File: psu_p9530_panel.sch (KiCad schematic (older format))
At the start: 56 parts, among them IC306 LTC1658, IC308 CD4052B, IC310 TLC272, IC312 TLC272, U401 74HCT164

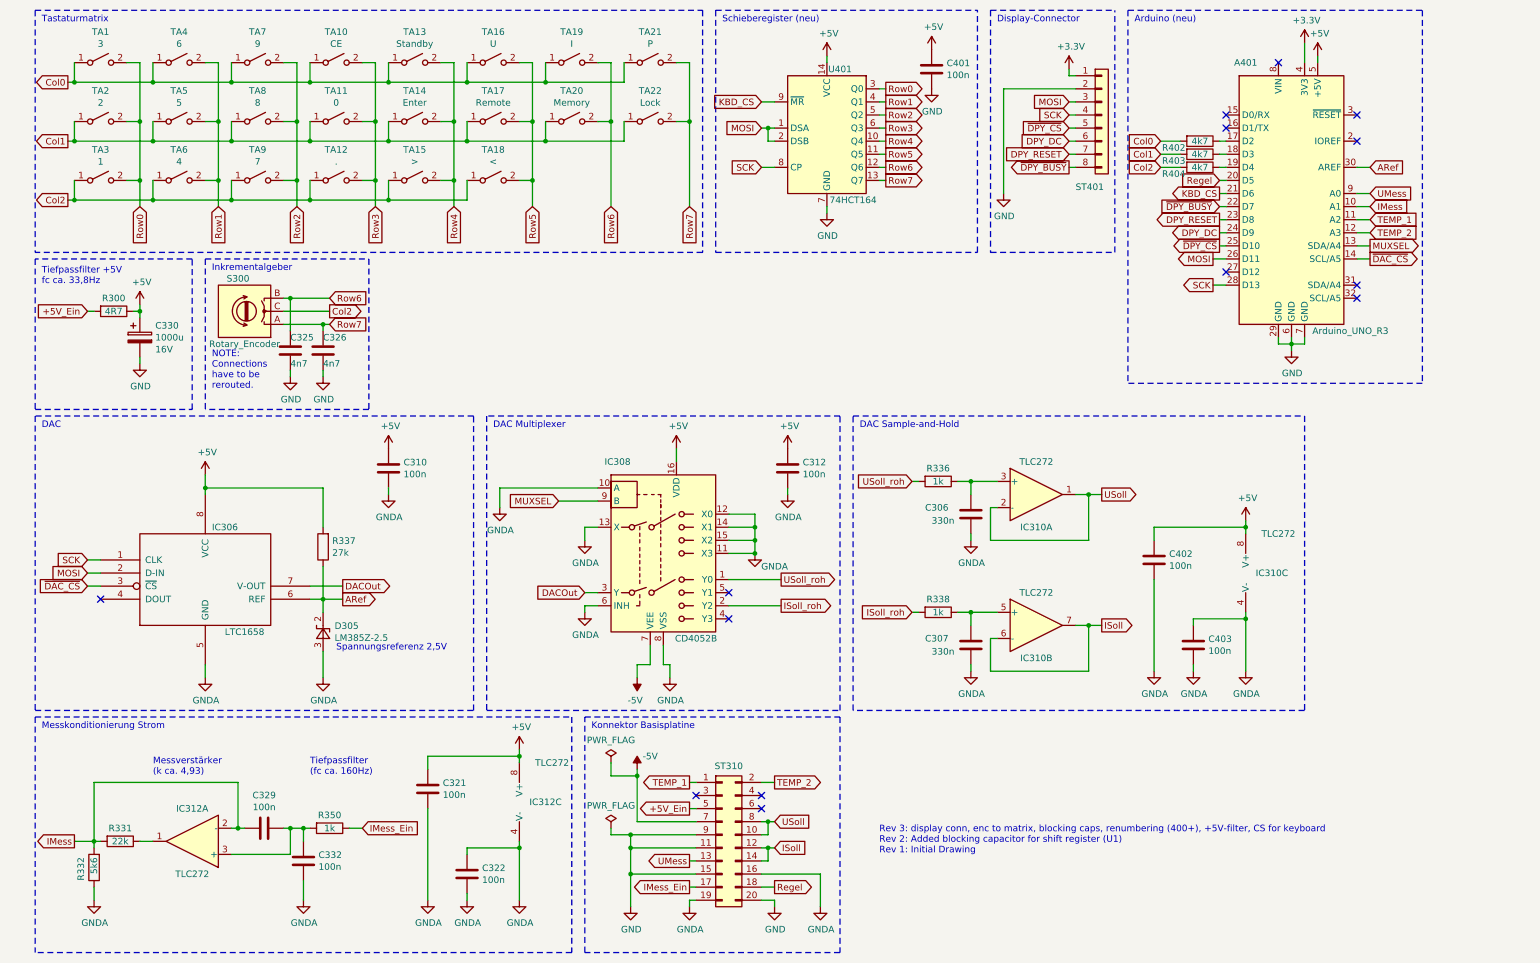
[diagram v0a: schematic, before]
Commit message: Beschreibung Original-Netzteil hinzugefügt, Übersetzung auf Deutsch, Digital GND für digitale Signale
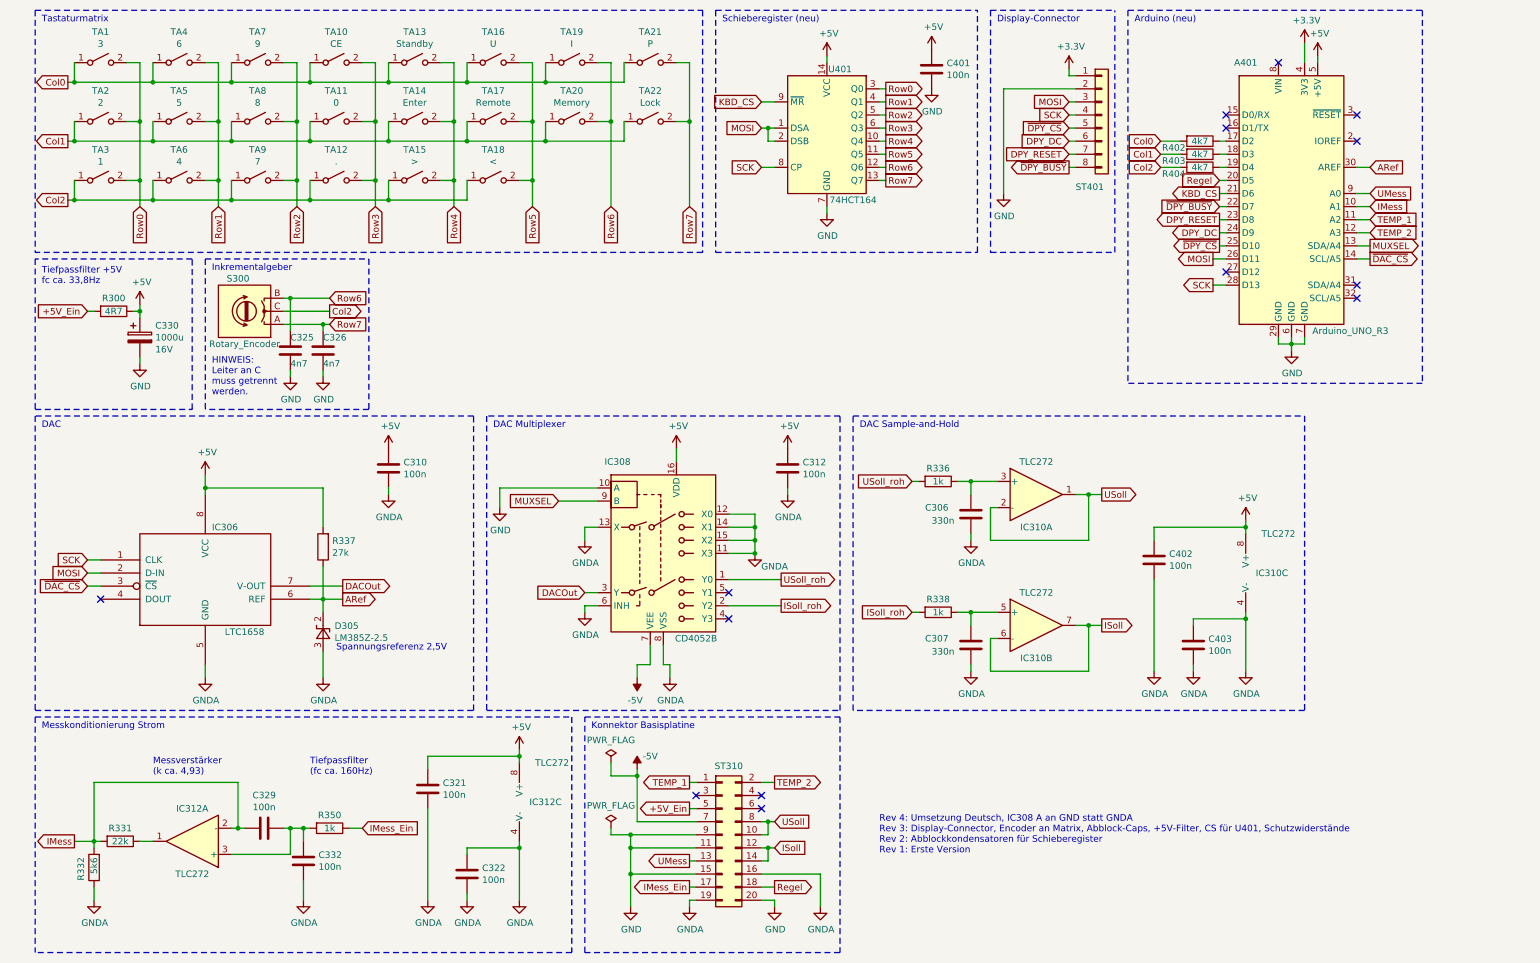
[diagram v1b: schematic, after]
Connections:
- net GND: now also IC308.10 (A)
- net GNDA: no longer IC308.10 (A)
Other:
- note added: "HINWEIS:\nLeiter an C\nmuss getrennt\nwerden."
- note added: "Rev 4: Umsetzung Deutsch, IC308 A an GND statt GNDA\nRev 3: Display-Connector, Encoder an Matrix, Abblock-Caps, +5V-Filter, CS für U401, Schutzwiderstände\nRev 2: Abblockkondensatoren für Schieberegister\nRev 1: Erste Version"
- note removed: "NOTE:\nConnections\nhave to be\nrerouted."
- note removed: "Rev 3: display conn, enc to matrix, blocking caps, renumbering (400+), +5V-filter, CS for keyboard\nRev 2: Added blocking capacitor for shift register (U1)\nRev 1: Initial Drawing"
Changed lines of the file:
@@
 encoding utf-8
 Sheet 1 1
-Title "ELV PS9530 Control Panel Replacement"
-Date "2022-08-06"
-Rev "3"
+Title "ELV PS9530 Ersatz Bedienteil"
+Date "2022-08-07"
+Rev "4"
 Comp "Ralf Gerlich"
 Comment1 ""
@@
 Text Notes 6850 3750 0    50   ~ 0
 DAC Sample-and-Hold
-$Comp
-L power:GNDA #PWR0120
-U 1 1 62F92CDD
-P 4100 4350
-F 0 "#PWR0120" H 4100 4100 50  0001 C CNN
-F 1 "GNDA" H 4105 4177 50  0000 C CNN
-F 2 "" H 4100 4350 50  0001 C CNN
-F 3 "" H 4100 4350 50  0001 C CNN
-	1    4100 4350
-	1    0    0    -1
-$EndComp
 Wire Wire Line
 	4100 4350 4100 4200
@@
 	1750 3600 1750 2450
 Text Notes 7000 7000 0    50   ~ 0
-Rev 3: display conn, enc to matrix, blocking caps, renumbering (400+), +5V-filter, CS for keyboard\nRev 2: Added blocking capacitor for shift register (U1)\nRev 1: Initial Drawing
+Rev 4: Umsetzung Deutsch, IC308 A an GND statt GNDA\nRev 3: Display-Connector, Encoder an Matrix, Abblock-Caps, +5V-Filter, CS für U401, Schutzwiderstände\nRev 2: Abblockkondensatoren für Schieberegister\nRev 1: Erste Version
 $Comp
 L Device:R R402
@@
 Wire Wire Line
 	2450 2850 2800 2850
-Text Notes 1900 3450 0    50   ~ 0
-NOTE:\nConnections\nhave to be\nrerouted.
+Text Notes 1900 3500 0    50   ~ 0
+HINWEIS:\nLeiter an C\nmuss getrennt\nwerden.
 Wire Notes Line
 	1850 2450 3100 2450
@@
 	4950 6850 4950 6800
 Connection ~ 5100 6850
+$Comp
+L power:GND #PWR?
+U 1 1 62F0FC79
+P 4100 4350
+F 0 "#PWR?" H 4100 4100 50  0001 C CNN
+F 1 "GND" H 4105 4177 50  0000 C CNN
+F 2 "" H 4100 4350 50  0001 C CNN
+F 3 "" H 4100 4350 50  0001 C CNN
+	1    4100 4350
+	1    0    0    -1
+$EndComp
 $EndSCHEMATC

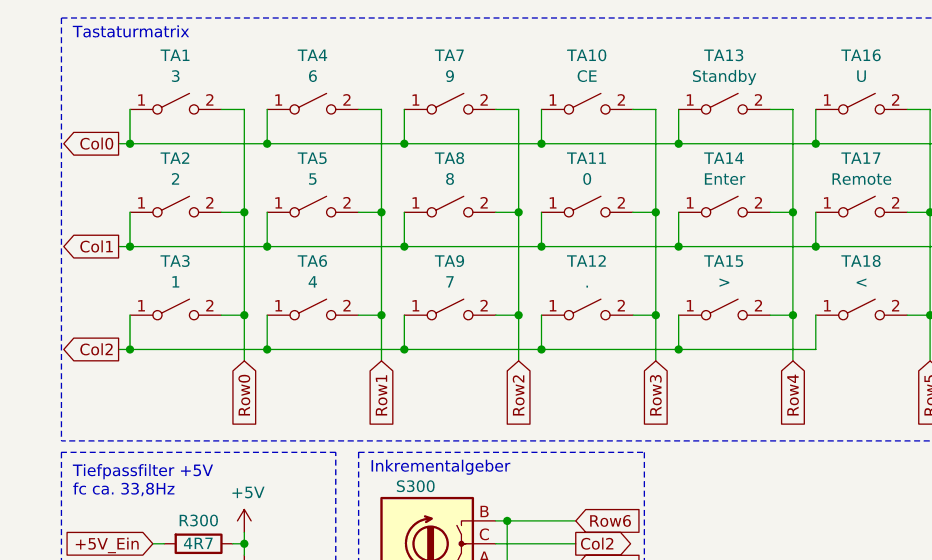
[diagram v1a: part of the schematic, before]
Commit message: Initial sketches for keyboard and e-paper tests
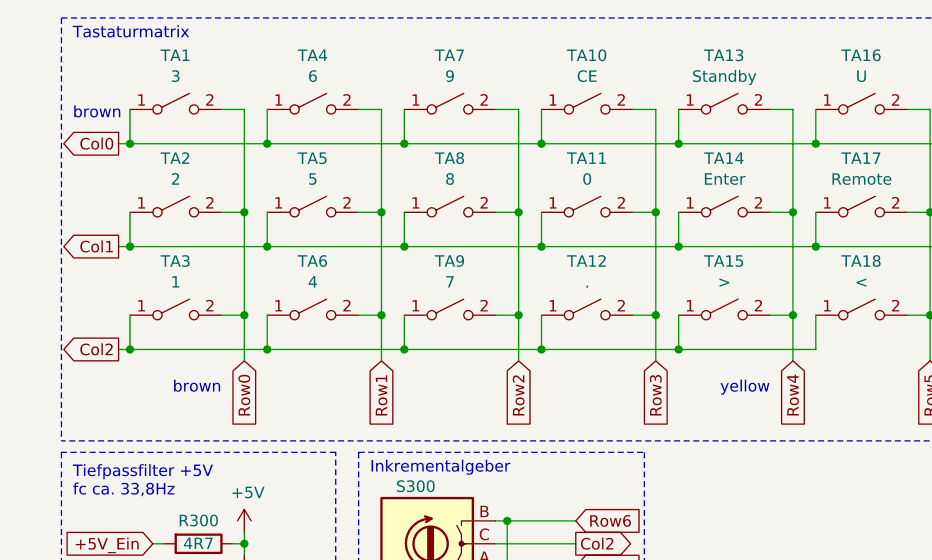
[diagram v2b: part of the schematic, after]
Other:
- note added: "brown"
- note added: "yellow"
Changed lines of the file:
@@
 	1    0    0    -1
 $EndComp
+Text Notes 1250 2200 2    50   ~ 0
+brown
+Text Notes 3650 2200 2    50   ~ 0
+yellow
+Text Notes 600  1000 0    50   ~ 0
+brown
 $EndSCHEMATC

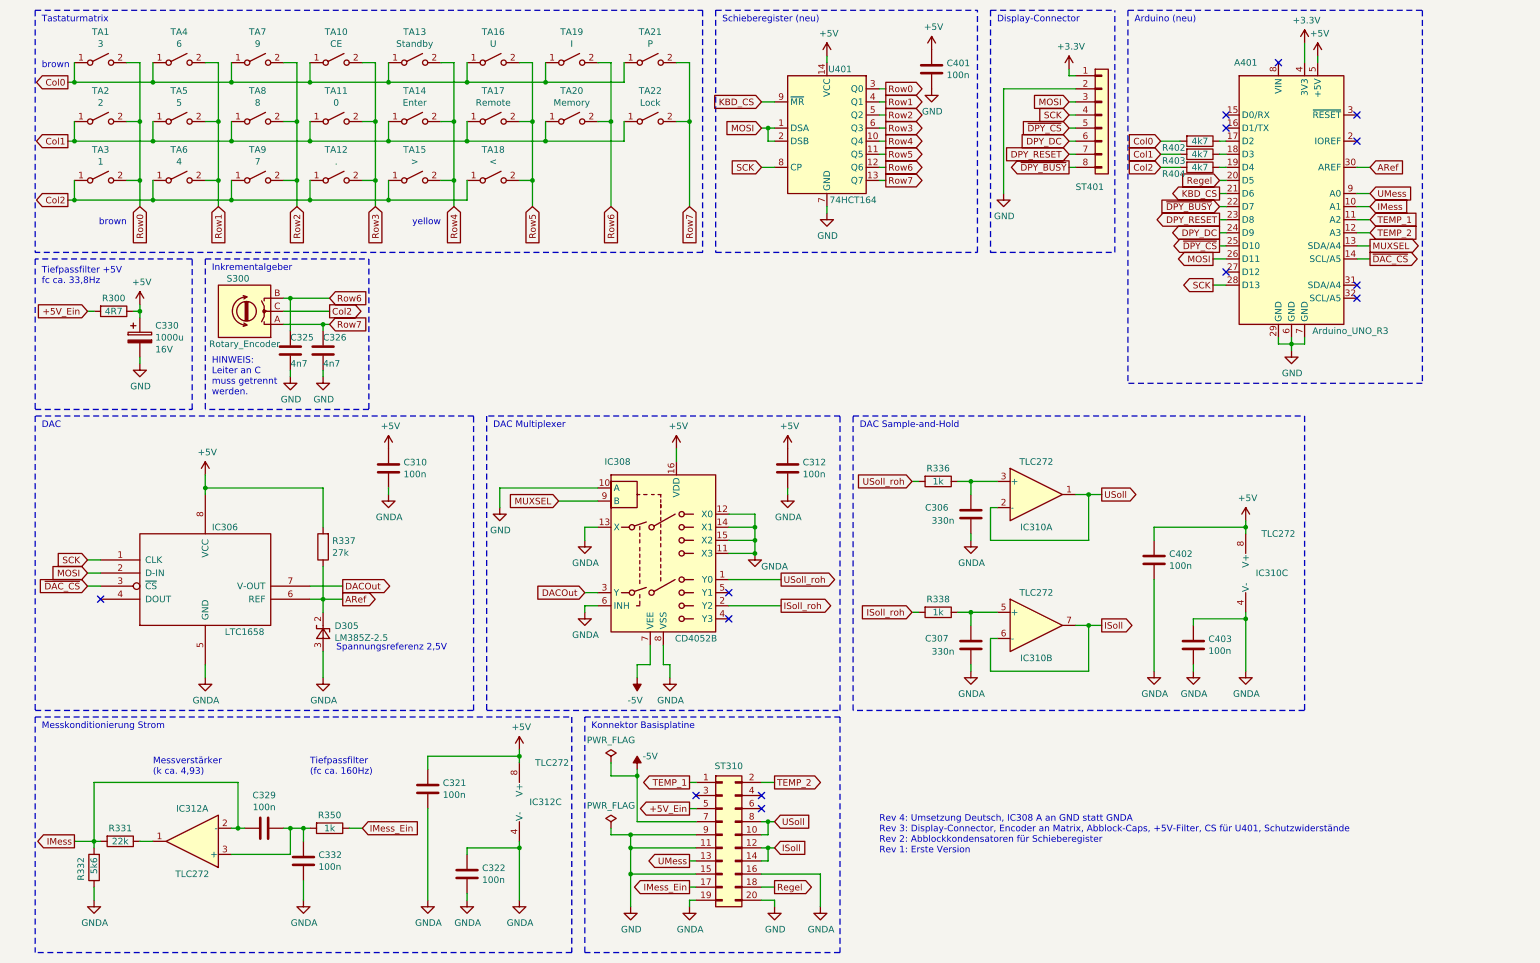
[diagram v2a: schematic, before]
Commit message: Test and document incremental encoder
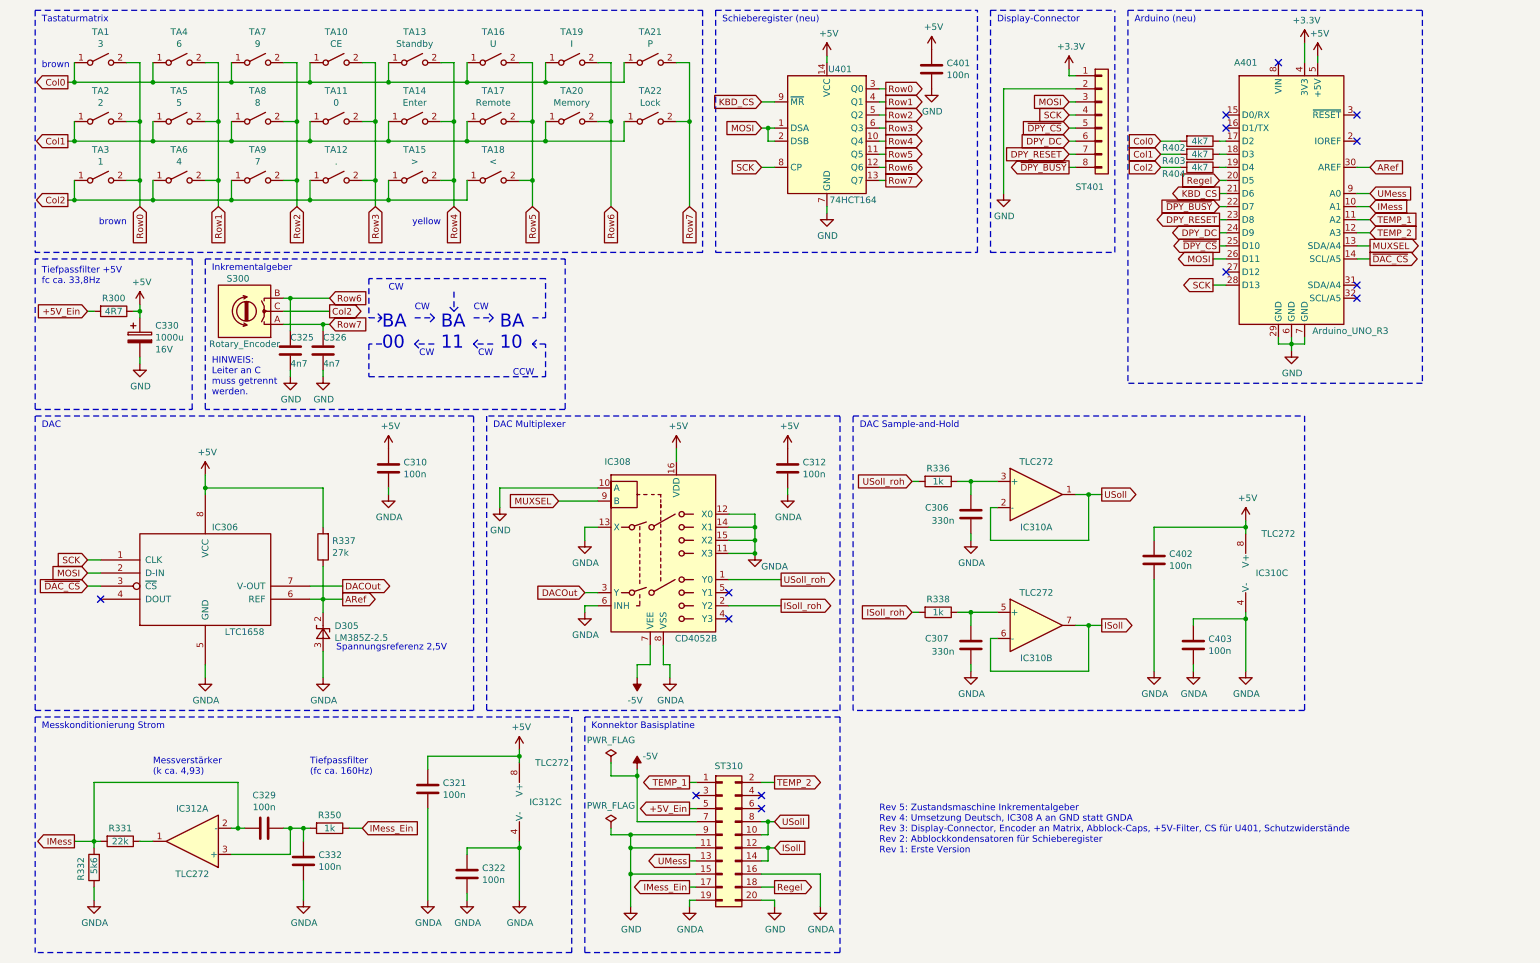
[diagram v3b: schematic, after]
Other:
- note added: "BA\n00"
- note added: "BA\n10"
- note added: "BA\n11"
- note added: "CCW"
- note added: "CW"
- note added: "Rev 5: Zustandsmaschine Inkrementalgeber\nRev 4: Umsetzung Deutsch, IC308 A an GND statt GNDA\nRev 3: Display-Connector, Encoder an Matrix, Abblock-Caps, +5V-Filter, CS für U401, Schutzwiderstände\nRev 2: Abblockkondensatoren für Schieberegister\nRev 1: Erste Version"
- note removed: "Rev 4: Umsetzung Deutsch, IC308 A an GND statt GNDA\nRev 3: Display-Connector, Encoder an Matrix, Abblock-Caps, +5V-Filter, CS für U401, Schutzwiderstände\nRev 2: Abblockkondensatoren für Schieberegister\nRev 1: Erste Version"
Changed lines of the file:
@@
 Sheet 1 1
 Title "ELV PS9530 Ersatz Bedienteil"
-Date "2022-08-07"
-Rev "4"
+Date "2022-08-12"
+Rev "5"
 Comp "Ralf Gerlich"
 Comment1 ""
@@
 	1750 3600 1750 2450
 Text Notes 7000 7000 0    50   ~ 0
-Rev 4: Umsetzung Deutsch, IC308 A an GND statt GNDA\nRev 3: Display-Connector, Encoder an Matrix, Abblock-Caps, +5V-Filter, CS für U401, Schutzwiderstände\nRev 2: Abblockkondensatoren für Schieberegister\nRev 1: Erste Version
+Rev 5: Zustandsmaschine Inkrementalgeber\nRev 4: Umsetzung Deutsch, IC308 A an GND statt GNDA\nRev 3: Display-Connector, Encoder an Matrix, Abblock-Caps, +5V-Filter, CS für U401, Schutzwiderstände\nRev 2: Abblockkondensatoren für Schieberegister\nRev 1: Erste Version
 $Comp
 L Device:R R402
@@
 Text Notes 1900 3500 0    50   ~ 0
 HINWEIS:\nLeiter an C\nmuss getrennt\nwerden.
-Wire Notes Line
-	1850 2450 3100 2450
-Wire Notes Line
-	3100 2450 3100 3600
-Wire Notes Line
-	3100 3600 1850 3600
 Wire Wire Line
 	9150 1550 9300 1550
@@
 Text Notes 600  1000 0    50   ~ 0
 brown
+Text Notes 3200 3150 0    100  ~ 0
+BA\n00
+Text Notes 4100 3150 0    100  ~ 0
+BA\n10
+Wire Notes Line style solid
+	3450 2900 3600 2900
+Wire Notes Line style solid
+	3600 2900 3550 2850
+Wire Notes Line style solid
+	3600 2900 3550 2950
+Text Notes 3450 2850 0    50   ~ 0
+CW
+Wire Notes Line style solid
+	4350 2900 4450 2900
+Wire Notes Line style solid
+	4450 2900 4450 2600
+Wire Notes Line style solid
+	4450 2600 3100 2600
+Wire Notes Line style solid
+	3100 2600 3100 2900
+Wire Notes Line style solid
+	3100 2900 3200 2900
+Wire Notes Line style solid
+	3200 2900 3150 2850
+Wire Notes Line style solid
+	3200 2900 3150 2950
+Wire Notes Line style solid
+	3200 3100 3100 3100
+Wire Notes Line style solid
+	3100 3100 3100 3350
+Wire Notes Line style solid
+	3100 3350 4450 3350
+Wire Notes Line style solid
+	4450 3350 4450 3100
+Wire Notes Line style solid
+	4450 3100 4350 3100
+Wire Notes Line style solid
+	4350 3100 4400 3050
+Wire Notes Line style solid
+	4350 3100 4400 3150
+Text Notes 3250 2700 0    50   ~ 0
+CW
+Text Notes 4200 3350 0    50   ~ 0
+CCW
+Wire Notes Line
+	1850 2450 4600 2450
+Wire Notes Line
+	4600 2450 4600 3600
+Wire Notes Line
+	4600 3600 1850 3600
+Wire Notes Line style solid
+	3900 2900 4050 2900
+Wire Notes Line style solid
+	4050 2900 4000 2850
+Wire Notes Line style solid
+	4050 2900 4000 2950
+Text Notes 3900 2850 0    50   ~ 0
+CW
+Text Notes 3650 3150 0    100  ~ 0
+BA\n11
+Wire Notes Line style solid
+	3600 3100 3450 3100
+Wire Notes Line style solid
+	3450 3100 3500 3150
+Wire Notes Line style solid
+	3450 3100 3500 3050
+Text Notes 3600 3200 2    50   ~ 0
+CW
+Wire Notes Line style solid
+	4050 3100 3900 3100
+Wire Notes Line style solid
+	3900 3100 3950 3150
+Wire Notes Line style solid
+	3900 3100 3950 3050
+Text Notes 4050 3200 2    50   ~ 0
+CW
+Wire Notes Line style solid
+	3750 2700 3750 2850
+Wire Notes Line style solid
+	3750 2850 3800 2800
+Wire Notes Line style solid
+	3750 2850 3700 2800
 $EndSCHEMATC
